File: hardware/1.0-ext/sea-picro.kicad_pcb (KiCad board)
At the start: 4 copper layers, 17.8 x 33 mm, 54 parts, among them J1 USB_C_Receptacle_USB2.0, J2 Sea-Picro, Q1 2N7002VC-7, Q2 2N7002VC-7, U1 XC6210B332MR-G, U2 GD25Q64CWIGR, U3 RP2040, U4 74LVC1T45, Y1 12MHz

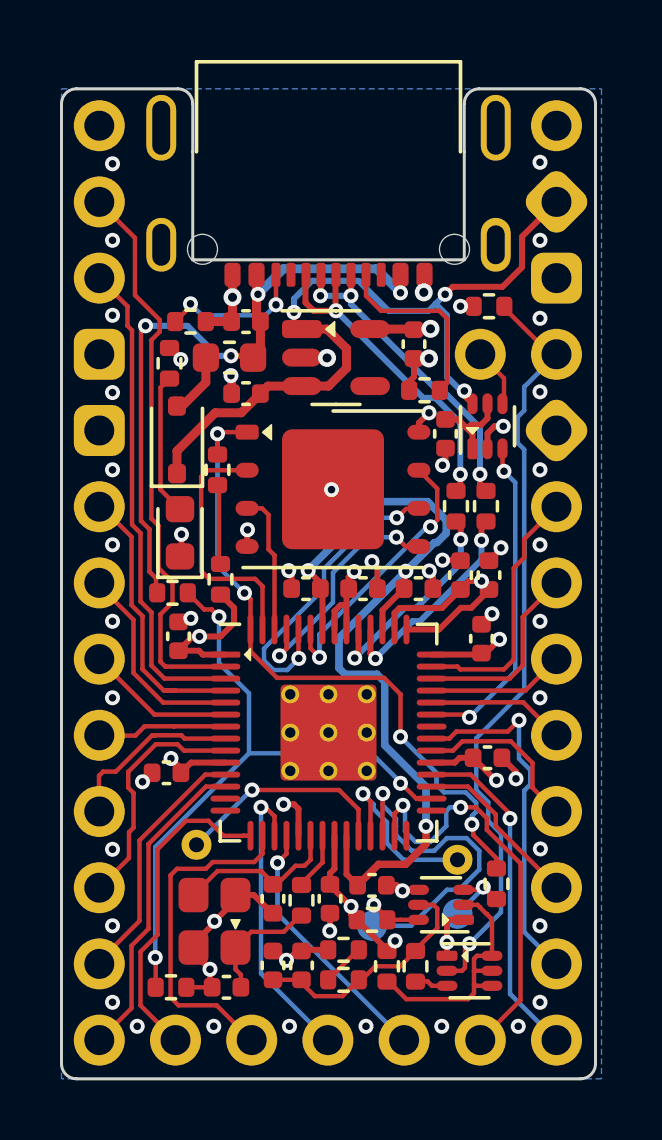
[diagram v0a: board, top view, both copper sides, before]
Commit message: fix trace width for level shifter
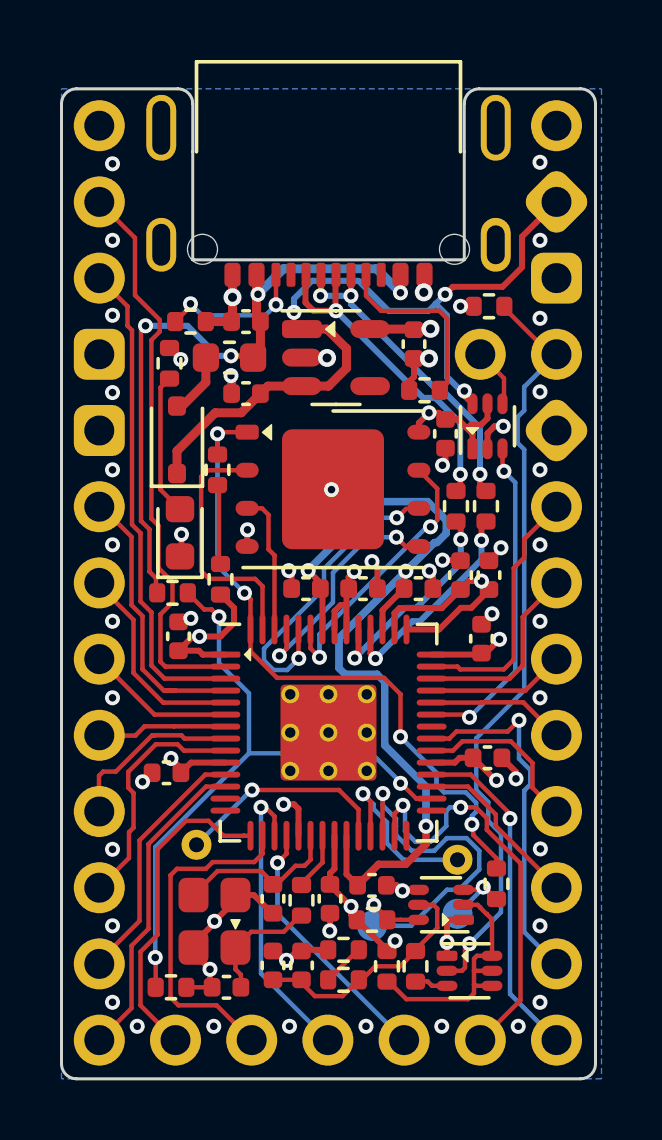
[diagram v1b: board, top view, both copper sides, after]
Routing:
- net +3V3: track 34.8 -> 35.4 mm
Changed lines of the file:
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@@
   (segment (start 126.4 92.21) (end 126.6 92.01) (width 0.2) (layer "F.Cu") (net 7))
   (segment (start 126.25 101.32) (end 126.25 101.351329) (width 0.2) (layer "F.Cu") (net 7))
+  (segment (start 129.88 85.6) (end 130.1 85.82) (width 0.2) (layer "F.Cu") (net 7))
   (segment (start 131 86.3) (end 130.825 86.125) (width 0.2) (layer "F.Cu") (net 7))
   (segment (start 121.28 97.6) (end 121.28 97.454012) (width 0.2) (layer "F.Cu") (net 7))
@@
   (segment (start 130.6 91.49) (end 130.88 91.21) (width 0.2) (layer "F.Cu") (net 7))
   (segment (start 129.6375 97.26) (end 130.41 97.26) (width 0.2) (layer "F.Cu") (net 7))
+  (segment (start 129.55 85.6) (end 129.88 85.6) (width 0.2) (layer "F.Cu") (net 7))
   (segment (start 131.3 93.61) (end 131.44 93.61) (width 0.2) (layer "F.Cu") (net 7))
   (segment (start 121.2 93.53) (end 121.674421 93.055579) (width 0.2) (layer "F.Cu") (net 7))
